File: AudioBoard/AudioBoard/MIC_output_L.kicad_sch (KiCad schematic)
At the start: 0 parts

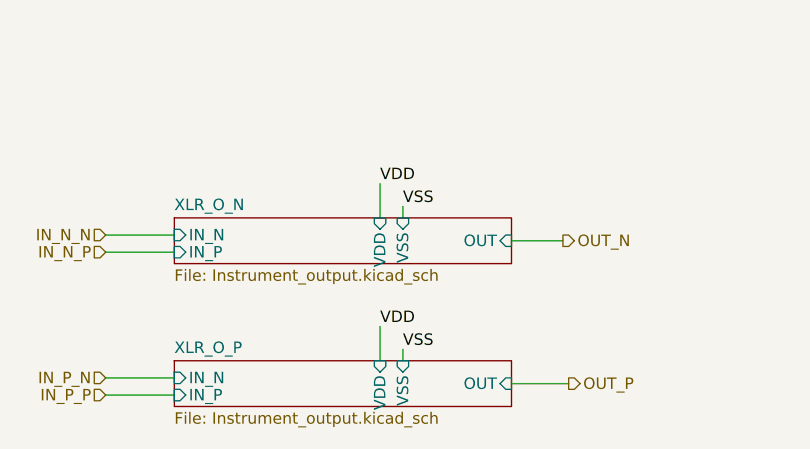
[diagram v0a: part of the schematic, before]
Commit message: xlr frontends added
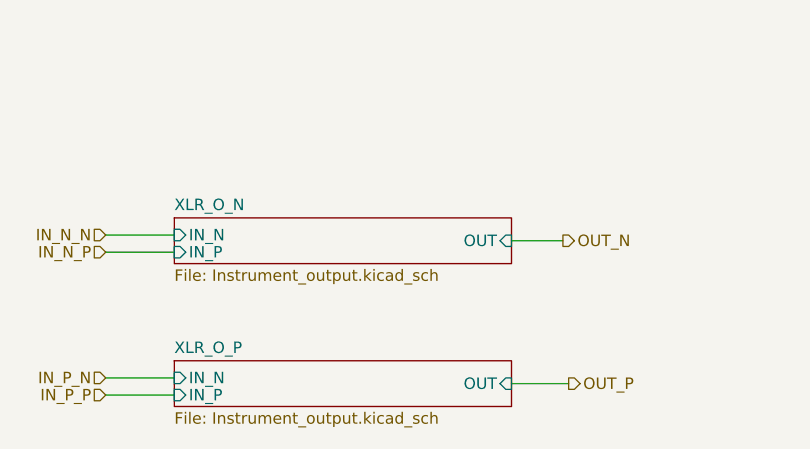
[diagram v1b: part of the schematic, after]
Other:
- sheet XLR_O_N ports: added none; removed VDD, VSS
- sheet XLR_O_P ports: added none; removed VDD, VSS
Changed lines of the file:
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@@
-	(wire
-		(pts
-			(xy 115.57 62.865) (xy 115.57 66.675)
-		)
-		(stroke
-			(width 0)
-			(type default)
-		)
-	)
 	(wire
 		(pts
@@
 	(wire
 		(pts
-			(xy 118.11 49.53) (xy 118.11 50.8)
-		)
-		(stroke
-			(width 0)
-			(type default)
-		)
-	)
-	(wire
-		(pts
 			(xy 85.09 54.61) (xy 92.71 54.61)
 		)
@@
 	(wire
 		(pts
-			(xy 115.57 46.99) (xy 115.57 50.8)
-		)
-		(stroke
-			(width 0)
-			(type default)
-		)
-	)
-	(wire
-		(pts
-			(xy 118.11 65.405) (xy 118.11 66.675)
-		)
-		(stroke
-			(width 0)
-			(type default)
-		)
-	)
-	(wire
-		(pts
 			(xy 48.895 27.305) (xy 55.88 27.305)
 		)
@@
 			(width 0)
 			(type default)
-		)
-	)
-	(label "VSS"
-		(at 118.11 65.405 0)
-		(effects
-			(font
-				(size 1.27 1.27)
-			)
-			(justify left bottom)
-		)
-	)
-	(label "VDD"
-		(at 115.57 46.99 0)
-		(effects
-			(font
-				(size 1.27 1.27)
-			)
-			(justify left bottom)
-		)
-	)
-	(label "VSS"
-		(at 118.11 49.53 0)
-		(effects
-			(font
-				(size 1.27 1.27)
-			)
-			(justify left bottom)
 		)
 	)
@@
 	(label "VDD"
 		(at 55.88 27.305 0)
-		(effects
-			(font
-				(size 1.27 1.27)
-			)
-			(justify left bottom)
-		)
-	)
-	(label "VDD"
-		(at 115.57 62.865 0)
 		(effects
 			(font
@@
 			)
 		)
-		(pin "VDD" input
-			(at 115.57 50.8 90)
-			(effects
-				(font
-					(size 1.27 1.27)
-				)
-				(justify right)
-			)
-		)
-		(pin "VSS" input
-			(at 118.11 50.8 90)
-			(effects
-				(font
-					(size 1.27 1.27)
-				)
-				(justify right)
-			)
-		)
 		(instances
 			(project "AudioBoard"
@@
 			(effects
 				(font
-					(size 1.27 1.27)
-				)
-				(justify right)
-			)
-		)
-		(pin "VDD" input
-			(at 115.57 66.675 90)
-			(effects
-				(font
-					(size 1.27 1.27)
-				)
-				(justify right)
-			)
-		)
-		(pin "VSS" input
-			(at 118.11 66.675 90)
-			(effects
-				(font

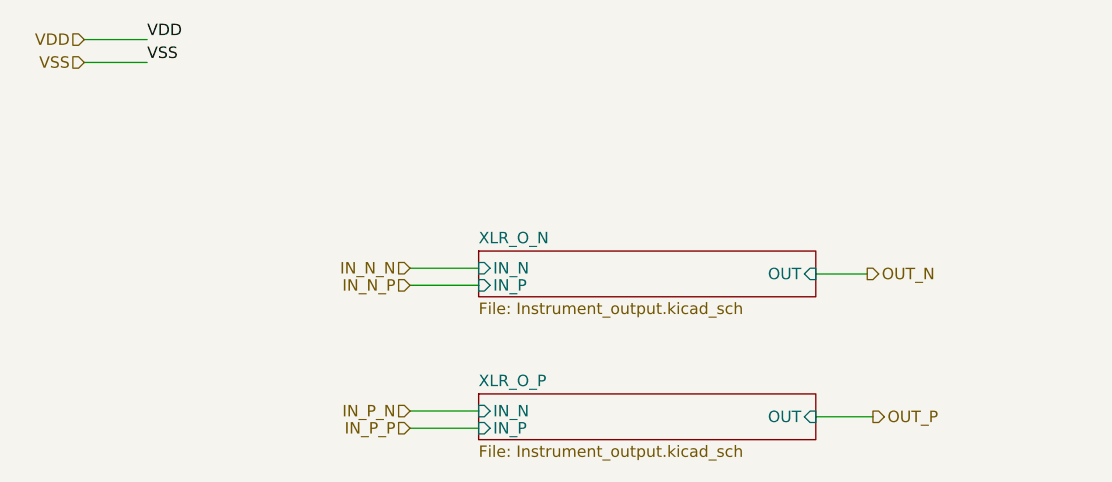
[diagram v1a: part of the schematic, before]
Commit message: added dxf file to pcb view
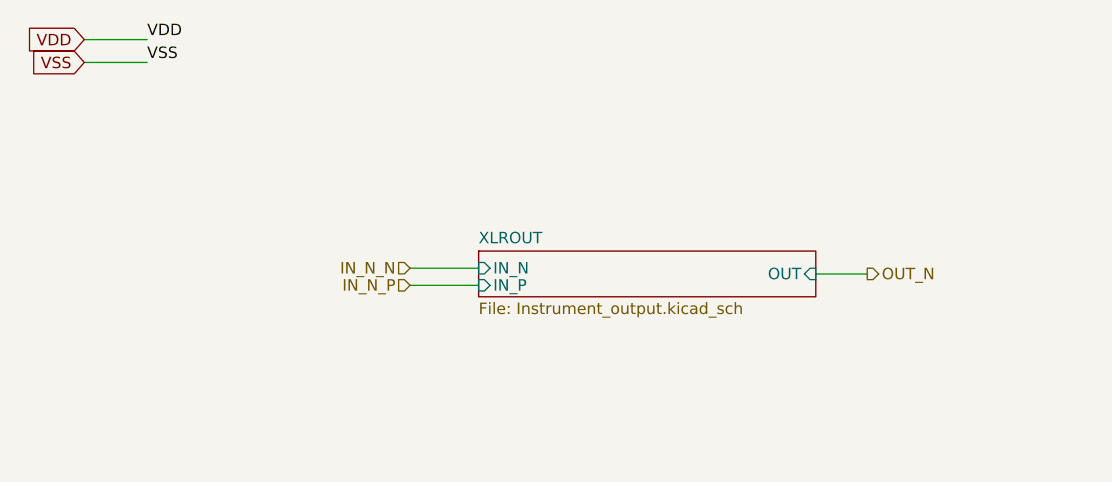
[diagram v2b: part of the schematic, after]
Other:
- sheet XLR_O_N renamed XLROUT
- removed sheet XLR_O_P
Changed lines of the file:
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@@
-	(wire
-		(pts
-			(xy 85.09 68.58) (xy 92.71 68.58)
-		)
-		(stroke
-			(width 0)
-			(type default)
-		)
-	)
 	(wire
 		(pts
 			(xy 328.93 38.735) (xy 335.915 38.735)
-		)
-		(stroke
-			(width 0)
-			(type default)
-		)
-	)
-	(wire
-		(pts
-			(xy 85.09 70.485) (xy 92.71 70.485)
-		)
-		(stroke
-			(width 0)
-			(type default)
-		)
-	)
-	(wire
-		(pts
-			(xy 136.525 69.215) (xy 130.175 69.215)
 		)
 		(stroke
@@
 		)
 	)
-	(hierarchical_label "IN_P_N"
-		(shape input)
-		(at 85.09 68.58 180)
-		(effects
-			(font
-				(size 1.27 1.27)
-			)
-			(justify right)
+	(global_label "VSS"
+		(shape input)
+		(at 48.895 29.845 180)
+		(fields_autoplaced yes)
+		(effects
+			(font
+				(size 1.27 1.27)
+			)
+			(justify right)
+		)
+		(property "Intersheetrefs" "${INTERSHEET_REFS}"
+			(at 42.4022 29.845 0)
+			(hide yes)
+			(show_name no)
+			(do_not_autoplace no)
+			(effects
+				(font
+					(size 1.27 1.27)
+				)
+				(justify right)
+			)
+		)
+	)
+	(global_label "VDD"
+		(shape input)
+		(at 48.895 27.305 180)
+		(fields_autoplaced yes)
+		(effects
+			(font
+				(size 1.27 1.27)
+			)
+			(justify right)
+		)
+		(property "Intersheetrefs" "${INTERSHEET_REFS}"
+			(at 42.2812 27.305 0)
+			(hide yes)
+			(show_name no)
+			(do_not_autoplace no)
+			(effects
+				(font
+					(size 1.27 1.27)
+				)
+				(justify right)
+			)
 		)
 	)
@@
 		(shape input)
 		(at 85.09 52.705 180)
-		(effects
-			(font
-				(size 1.27 1.27)
-			)
-			(justify right)
-		)
-	)
-	(hierarchical_label "VDD"
-		(shape input)
-		(at 48.895 27.305 180)
 		(effects
 			(font
@@
 		)
 	)
-	(hierarchical_label "IN_P_P"
-		(shape input)
-		(at 85.09 70.485 180)
-		(effects
-			(font
-				(size 1.27 1.27)
-			)
-			(justify right)
-		)
-	)
-	(hierarchical_label "VSS"
-		(shape input)
-		(at 48.895 29.845 180)
-		(effects
-			(font
-				(size 1.27 1.27)
-			)
-			(justify right)
-		)
-	)
 	(hierarchical_label "IN_N_P"
 		(shape input)
@@
 			)
 			(justify right)
-		)
-	)
-	(hierarchical_label "OUT_P"
-		(shape output)
-		(at 136.525 69.215 0)
-		(effects
-			(font
-				(size 1.27 1.27)
-			)
-			(justify left)
 		)
 	)
@@
 			(color 0 0 0 0)
 		)
-		(property "Sheetname" "XLR_O_N"
+		(property "Sheetname" "XLROUT"
 			(at 92.71 50.0884 0)
 			(show_name no)
@@
 					(page "18")
 				)
-				(path "/dd5d876d-fff7-4cb4-baee-a023036d12ae/dc93ab06-88a8-4a45-be5a-487cdf5783e9"
-					(page "19")
-				)
-			)
-		)
-	)
-	(sheet
-		(at 92.71 66.675)
-		(size 37.465 5.08)
-		(exclude_from_sim no)
-		(in_bom yes)
-		(on_board yes)
-		(dnp no)
-		(fields_autoplaced yes)
-		(stroke
-			(width 0.1524)
-			(type solid)
-		)
-		(fill
-			(color 0 0 0 0)
-		)
-		(property "Sheetname" "XLR_O_P"
-			(at 92.71 65.9634 0)
-			(show_name no)
-			(do_not_autoplace no)
-			(effects
-				(font
-					(size 1.27 1.27)
-				)
-				(justify left bottom)
-			)
-		)
-		(property "Sheetfile" "Instrument_output.kicad_sch"
-			(at 92.71 72.3396 0)
-			(show_name no)
-			(do_not_autoplace no)
-			(effects
-				(font
-					(size 1.27 1.27)
-				)
-				(justify left top)
-			)
-		)
-		(pin "IN_N" input
-			(at 92.71 68.58 180)
-			(effects
-				(font
-					(size 1.27 1.27)
-				)
-				(justify left)
-			)
-		)
-		(pin "IN_P" input
-			(at 92.71 70.485 180)
-			(effects
-				(font
-					(size 1.27 1.27)
-				)
-				(justify left)
-			)
-		)
-		(pin "OUT" input
-			(at 130.175 69.215 0)
-			(effects
-				(font
-					(size 1.27 1.27)
-				)
-				(justify right)
-			)
-		)
-		(instances
-			(project "AudioBoard"
-				(path "/dd5d876d-fff7-4cb4-baee-a023036d12ae/e87fe4e0-dcc3-4a3a-a2f4-db36aaf0ad2f"
+				(path "/dd5d876d-fff7-4cb4-baee-a023036d12ae/dd7e807f-4b4f-494a-93a3-54e0064135c8"
 					(page "16")
 				)
-				(path "/dd5d876d-fff7-4cb4-baee-a023036d12ae/dc93ab06-88a8-4a45-be5a-487cdf5783e9"
-					(page "17")
-				)
-			)
+			)
